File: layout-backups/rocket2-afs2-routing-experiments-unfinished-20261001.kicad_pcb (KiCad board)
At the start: 2 copper layers, 54 x 54 mm, 51 parts, among them J1 ARM Cortex Debug, J3 XT60 POWER, U1 STM32F105RCT6, U2 LD1086DT33TR, U4 USBLC6-2SC6, U5 ADXL383, Y1 8MHz

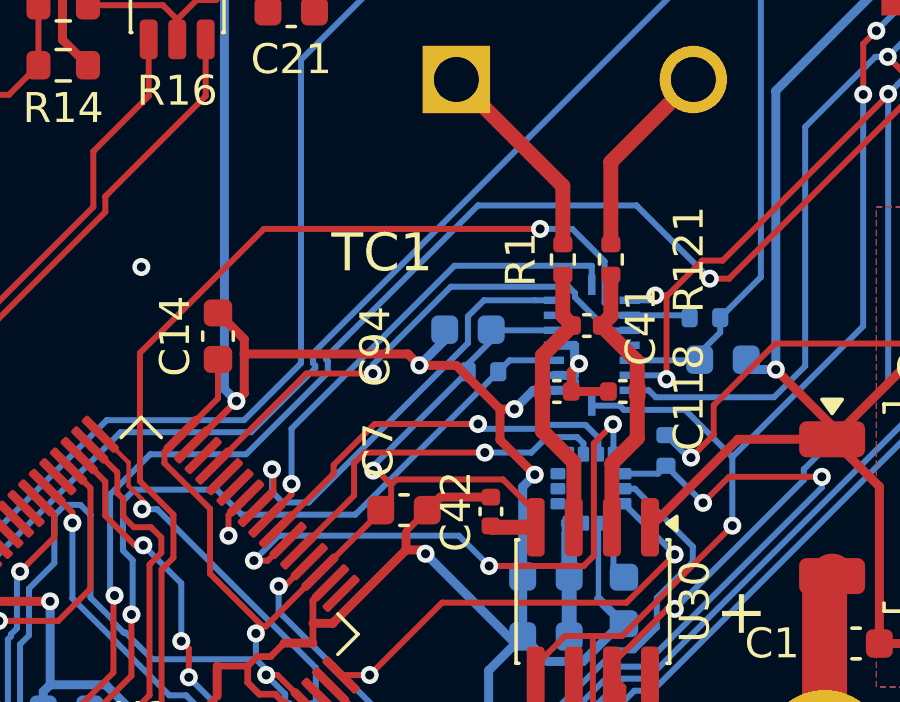
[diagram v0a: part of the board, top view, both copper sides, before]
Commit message: Save compact AFS2 layout and two-layer routing work in progress
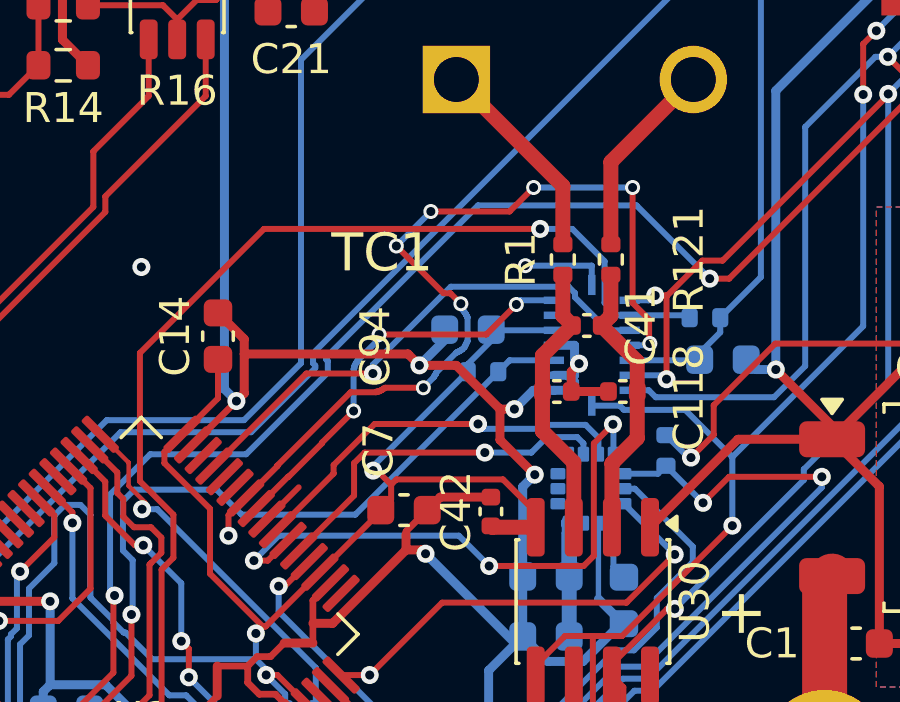
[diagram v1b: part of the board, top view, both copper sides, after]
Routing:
- net /IMU_INT3: track 1.50 -> 30.3 mm, vias 1 -> 8
- net /IMU_INT1: track 16.3 -> 4.36 mm
- net /IMU_INT2: track 15.2 -> 13.8 mm, vias 1 -> 3
